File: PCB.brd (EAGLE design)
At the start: 45.3 x 36 mm, 27 parts, among them U1 MSP430G2553_PW_20, U2 DRV8833_PWP_16, U3 DRV8833_PWP_16

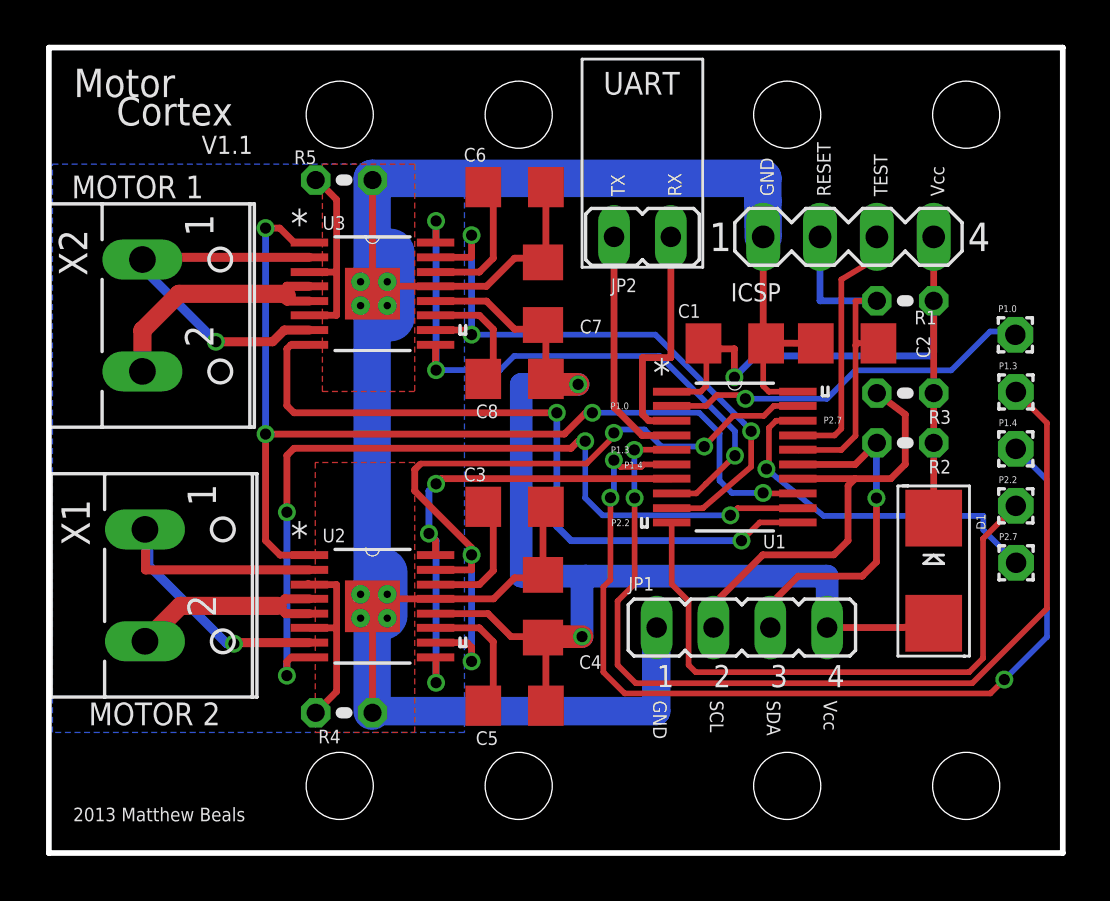
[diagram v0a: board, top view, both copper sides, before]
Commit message: Magor version revision
Fixed timer pinout problem
updated silk screen with new logo
broke out power and data to different headers
reworked MCU power isolation
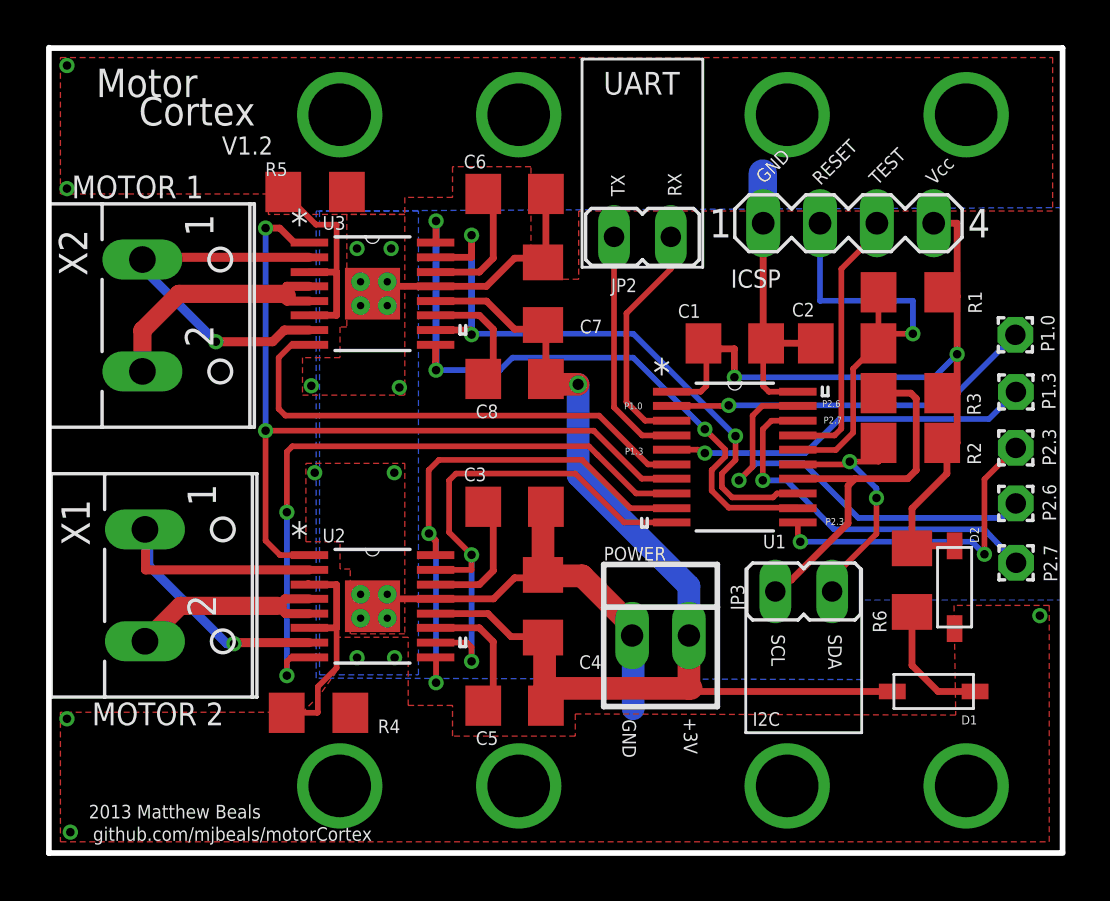
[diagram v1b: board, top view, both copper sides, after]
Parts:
- removed JP1: (no value), jumper:JP4
- removed P1.4, P2.2: (no value), wirepad:1,6/0,9
- added D2: (no value), adafruit:SOD-123
- added JP3: (no value), jumper:JP1
- added P2.3, P2.6: (no value), wirepad:1,6/0,9
- added POWER: 22-23-2021, con-molex:22-23-2021
- added R6: (no value), adafruit:R1206
- D1: device adafruit:SMADIODE -> adafruit:SOD-123
- R1, R2, R3, R4, R5: device adafruit:0204V -> adafruit:R1206
- moved D1 5.40 mm to (49.5, 51.2), turned to 180 degrees
- moved R5 1.40 mm to (21.9, 73.5)
- moved R4 1.14 mm to (22.1, 50.3)
- moved ICSP 0.61 mm to (45.7, 72.1)
- moved R1 0.44 mm to (48.5, 69.1)
- moved C6 0.30 mm to (30.8, 73.5)
- moved R2 0.23 mm to (48.5, 62.3)
- moved R3 0.23 mm to (48.5, 64.6)
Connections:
- removed net P1.4: P1.4.1, U1.6
- removed net P2.2: P2.2.1, U1.10
- new net +3V3UNREG: D1.C, R6.1
- new net P2.3: P2.3.1, U1.11
- new net P2.6: P2.6.1, U1.19
- net +3V3: now also D2.C, R6.2; no longer D1.C
- net +3V3MOTOR: now also POWER.2; no longer JP1.4
- net GND: now also D2.A, POWER.1; no longer JP1.1
- net N1ERROR: now also U1.8; no longer U1.12
- net N1IN1: now also U1.9; no longer U1.7
- net N1IN2: now also U1.10; no longer U1.19
- net N2ERROR: now also U1.6; no longer U1.11
- net N2IN1: now also U1.12; no longer U1.8
- net N2IN2: now also U1.13; no longer U1.9
- net NRESET: now also U1.7; no longer U1.13
- net SCL: now also JP3.1; no longer JP1.2
- net SDA: now also JP3.2; no longer JP1.3
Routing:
- net GND: track 108.4 -> 45.2 mm, vias 0 -> 21
- net P1.4: track 42.7 -> 0.00 mm, vias 3 -> 0
- net P2.2: track 27.7 -> 0.00 mm
- net P1.3: track 42.8 -> 16.6 mm, vias 2 -> 1
- net P2.6: track 0.00 -> 19.3 mm, vias 0 -> 1
- net P2.3: track 0.00 -> 14.7 mm, vias 0 -> 2
- net N2ERROR: track 32.3 -> 22.5 mm, vias 2 -> 0
- net N1IN2: track 33.3 -> 24.1 mm, vias 4 -> 2
- net NRESET: track 45.4 -> 37.5 mm, vias 4 -> 2
- net N1ERROR: track 37.7 -> 29.9 mm, vias 4 -> 2
- net +3V3: track 30.5 -> 37.2 mm, vias 1 -> 2
- net +3V3UNREG: track 0.00 -> 5.69 mm
- net RST: track 16.3 -> 20.7 mm, vias 0 -> 1
- net SDA: track 15.8 -> 11.6 mm, vias 1 -> 2
- net +3V3MOTOR: track 55.5 -> 52.4 mm, vias 2 -> 1
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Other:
- outline, holes or cut-outs redrawn
- board text added: "+3V"
- board text added: "I2C"
- board text added: "P2.3"
- board text added: "P2.6"
- board text added: "V1.2"
- board text added: "github.com/mjbeals/motorCortex"
- board text removed: "P1.4"
- board text removed: "P2.2"
- board text removed: "V1.1"

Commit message: Updated power managment
Added LDO for mcu power
Added buffered voltage divider to allow mcu to measure rail voltage
Repurposed P1.0 to measure rail voltage
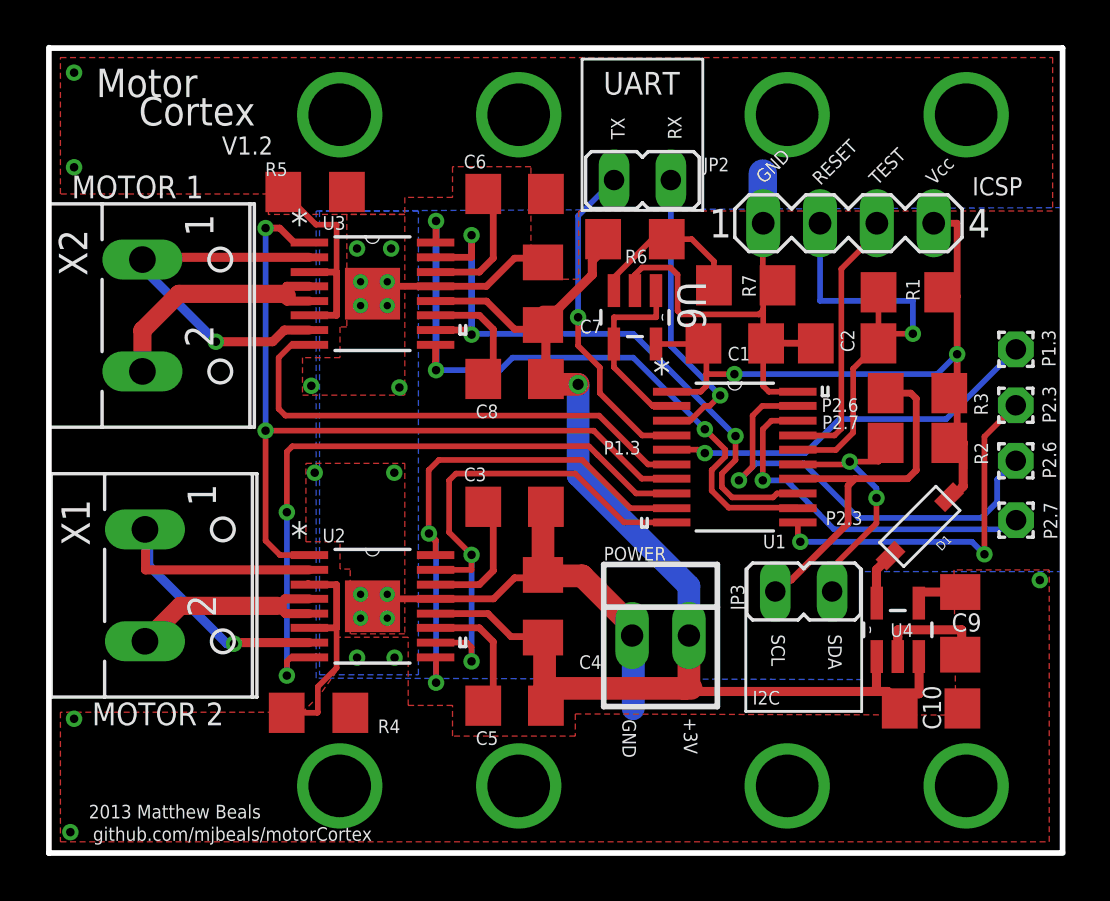
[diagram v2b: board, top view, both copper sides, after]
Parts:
- removed D2: (no value), adafruit:SOD-123
- removed P1.0: (no value), wirepad:1,6/0,9
- added C10, C9: (no value), adafruit:C1206
- added R7: 250k, adafruit:R1206
- added U4: REG101-3_DBV_5, TI:DBV5
- added U6: TLV2241_DBV_5, TI:DBV5
- R6: value (none) -> 500k
- moved R6 19.6 mm to (36.2, 71.4), turned to 180 degrees
- moved D1 7.40 mm to (48.9, 58.6), turned to 225 degrees
- moved JP2 2.54 mm to (36.5, 74.1)
- moved P1.3 1.91 mm to (53.2, 66.5)
- moved P2.6 1.91 mm to (53.2, 61.5)
- moved P2.7 1.91 mm to (53.2, 58.9)
- moved P2.3 1.90 mm to (53.2, 64.0)
- moved R2 0.32 mm to (48.8, 62.3)
- moved R3 0.32 mm to (48.8, 64.6)
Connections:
- removed net +3V3MOTOR: C4.2, C5.1, C7.2, C8.1, D1.A, POWER.2, U2.12, U3.12
- removed net +3V3UNREG: D1.C, R6.1
- removed net P1.0: P1.0.1, U1.2
- new net 3VOUT: D1.A, U4.5
- new net N$1: C9.2, U4.4
- new net VCC: C10.1, C4.2, C5.1, C7.2, C8.1, POWER.2, R6.2, U2.12, U3.12, U4.1, U4.3
- new net VSENSE_IN: R6.1, R7.2, U6.3
- new net VSENSE_OUT: U1.2, U6.1, U6.4
- net +3V3: now also D1.C, U6.5; no longer D2.C, R6.2
- net GND: now also C10.2, C9.1, R7.1, U4.2, U6.2; no longer D2.A
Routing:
- net VCC: track 0.00 -> 63.1 mm, vias 0 -> 1
- net +3V3MOTOR: track 52.4 -> 0.00 mm, vias 1 -> 0
- net P1.0: track 16.7 -> 0.00 mm, vias 1 -> 0
- net GND: track 45.2 -> 56.9 mm
- net VSENSE_OUT: track 0.00 -> 8.63 mm
- net VSENSE_IN: track 0.00 -> 7.58 mm
- net +3V3UNREG: track 5.69 -> 0.00 mm
- net UART_TX: track 10.7 -> 14.6 mm, vias 0 -> 1
- net +3V3: track 37.2 -> 33.4 mm
- net UART_RX: track 10.6 -> 13.2 mm, vias 0 -> 1
- net 3VOUT: track 0.00 -> 2.39 mm
- net N$1: track 0.00 -> 2.35 mm
- net P2.3: track 14.7 -> 16.6 mm
- net P2.6: track 19.3 -> 20.7 mm
- net P1.3: track 16.6 -> 17.3 mm
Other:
- board text removed: "P1.0"
